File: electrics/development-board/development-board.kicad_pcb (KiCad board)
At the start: 2 copper layers, 153 x 77 mm, 103 parts, among them J1 East, J10 Ext_5V, J2 Screw_Terminal, J3 USB_B, J4 Keyboard, J5 Mouse, J6 Audio, J7 VGA, J8 West, J9 PinOut, Q1 MMBT3904, Q2 MMBT3904, Q3 S8050, Q4 S8050, SW1 Reset, SW2 Setup, SW3 Power, U1 LD1117S33, U2 FT2232HL, U3 93C46-WMN6TP, U4 LTV-817S, U5 LTV-817S, U6 MAX3486, U7 SN74CBT16292, U8 SN74CBT16292, Y1 12MHz

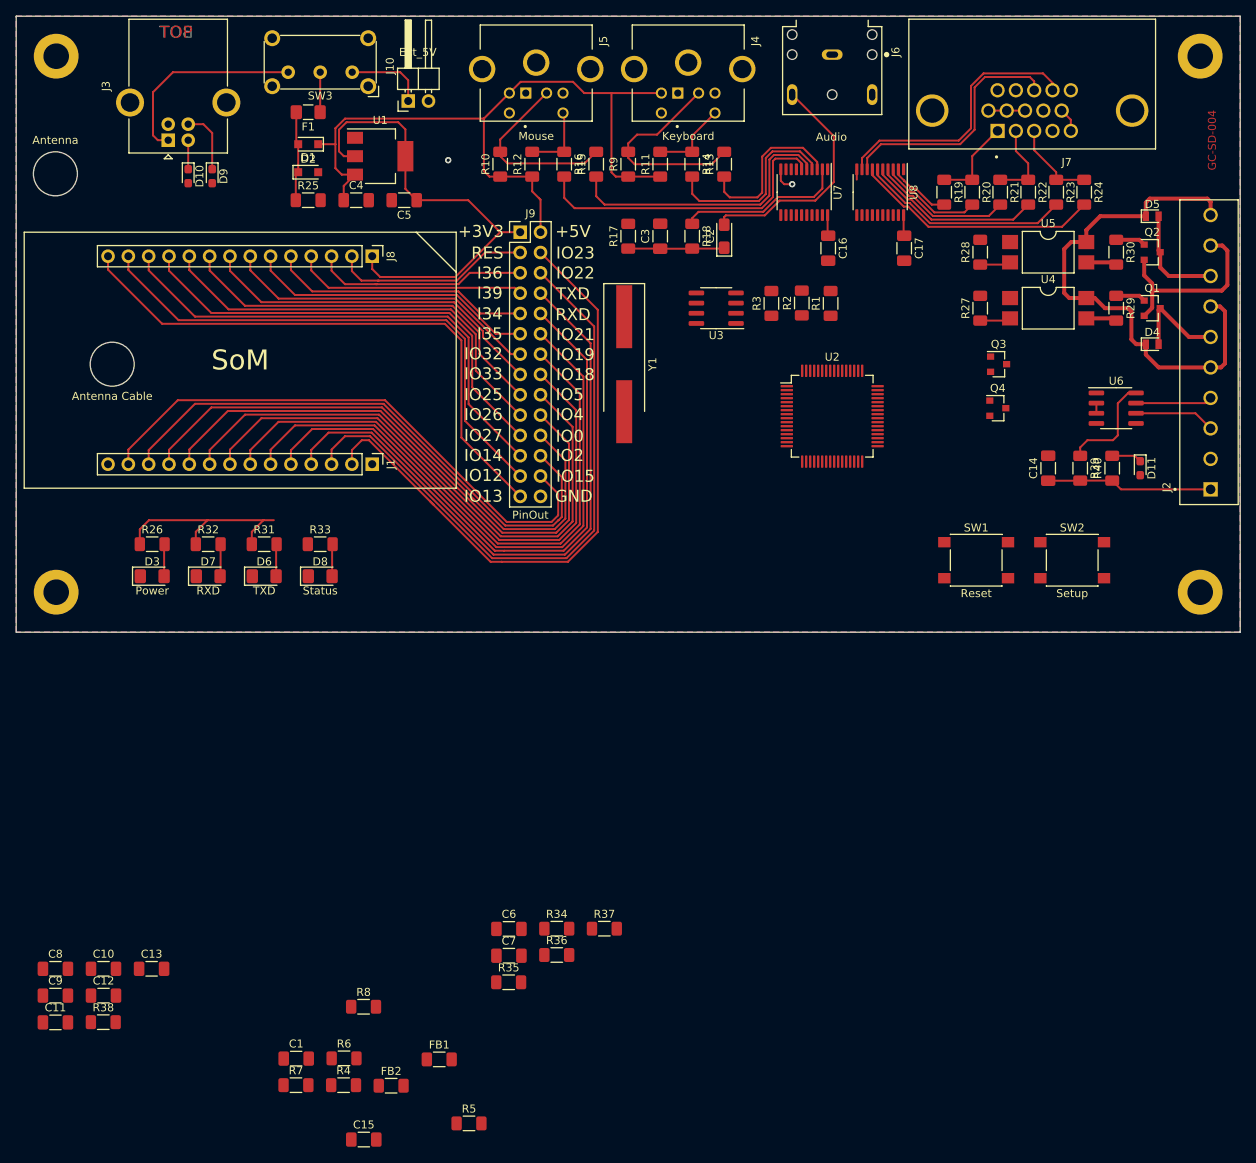
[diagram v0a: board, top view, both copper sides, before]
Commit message: Fix all ERC and DRC warnings during build
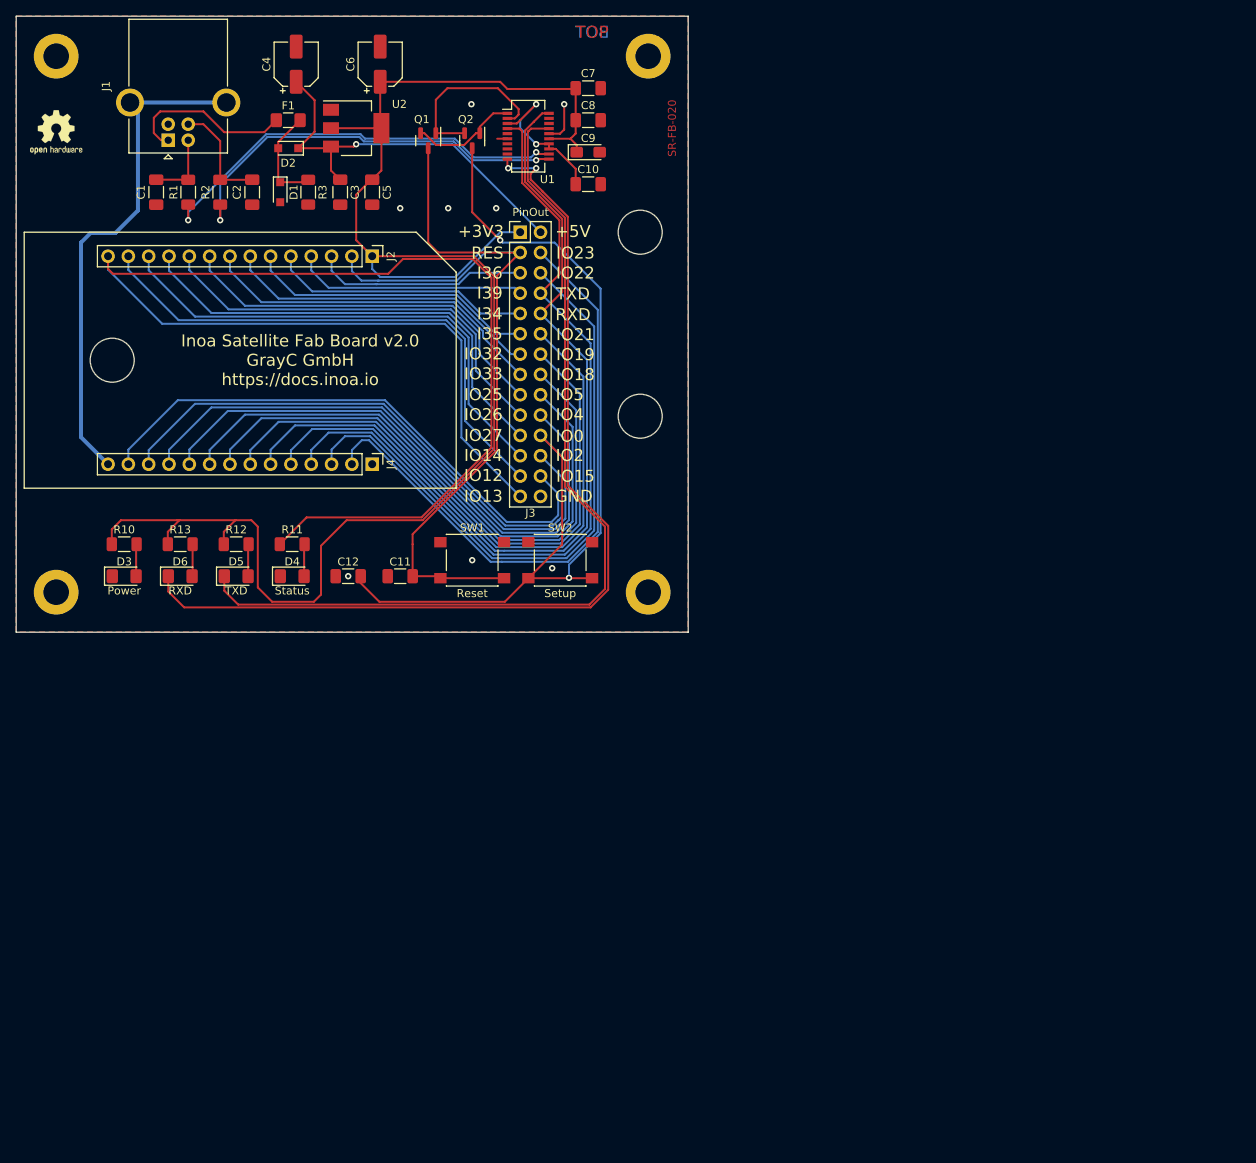
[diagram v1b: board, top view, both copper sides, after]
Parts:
- removed the C11 at (54.9, 175.8)
- removed the C12 at (60.9, 172.4)
- removed C13: 0u1, Capacitor_SMD:C_1206_3216Metric_Pad1.33x1.80mm_HandSolder
- removed C14, C15, C16, C17: 100nF, Capacitor_SMD:C_1206_3216Metric_Pad1.33x1.80mm_HandSolder
- removed the C3 at (130.5, 77.5)
- removed D10, D11, D9: D_TVS, Diode_SMD:D_0603_1608Metric_Pad1.05x0.95mm_HandSolder
- removed the D4 at (192.0, 91.0)
- removed the D5 at (192.0, 75.0)
- removed FB1, FB2: 1k@100MHz, Resistor_SMD:R_1206_3216Metric_Pad1.30x1.75mm_HandSolder
- removed J10: Ext_5V, Connector_PinHeader_2.54mm:PinHeader_1x02_P2.54mm_Horizontal
- removed the J2 at (199.3, 92.0)
- removed the J3 at (69.0, 65.5)
- removed the J4 at (134.0, 55.8)
- removed J5: Mouse, footprints:TE_5749180-1
- removed J6: Audio, footprints:CUI_SJ1-3523N
- removed J7: VGA, footprints:AMPHENOL_L77HDE15SD1CH4F
- removed Q3, Q4: S8050, Package_TO_SOT_SMD:SOT-23
- removed the R10 at (110.5, 68.5)
- removed the R11 at (130.5, 68.5)
- removed the R12 at (114.5, 68.5)
- removed the R13 at (138.5, 68.5)
- removed R14, R15, R16: 120R, Resistor_SMD:R_1206_3216Metric_Pad1.30x1.75mm_HandSolder
- removed R17: 150R, Resistor_SMD:R_1206_3216Metric_Pad1.30x1.75mm_HandSolder
- removed R18: 270R, Resistor_SMD:R_1206_3216Metric_Pad1.30x1.75mm_HandSolder
- removed R19, R21, R23: 400R, Resistor_SMD:R_1206_3216Metric_Pad1.30x1.75mm_HandSolder
- removed R20, R22, R24: 800R, Resistor_SMD:R_1206_3216Metric_Pad1.30x1.75mm_HandSolder
- removed R27, R28, R29, R30: 220R, Resistor_SMD:R_1206_3216Metric_Pad1.30x1.75mm_HandSolder
- removed the R3 at (144.4, 85.9)
- removed R34, R35, R36, R37, R4, R5, R7: 10k, Resistor_SMD:R_1206_3216Metric_Pad1.30x1.75mm_HandSolder
- removed R38: 12k, Resistor_SMD:R_1206_3216Metric_Pad1.30x1.75mm_HandSolder
- removed R39, R40: R, Resistor_SMD:R_1206_3216Metric_Pad1.30x1.75mm_HandSolder
- removed R6: 2k2, Resistor_SMD:R_1206_3216Metric_Pad1.30x1.75mm_HandSolder
- removed R8: 0R, Resistor_SMD:R_1206_3216Metric_Pad1.30x1.75mm_HandSolder
- removed R9: 2k, Resistor_SMD:R_1206_3216Metric_Pad1.30x1.75mm_HandSolder
- removed SW3: Power, Button_Switch_THT:SW_E-Switch_EG1224_SPDT_Angled
- removed U3: 93C46-WMN6TP, Package_SO:SOIC-8_3.9x4.9mm_P1.27mm
- removed U4, U5: LTV-817S, Package_DIP:SMDIP-4_W9.53mm
- removed U6: MAX3486, Package_SO:SOIC-8_3.9x4.9mm_P1.27mm
- removed U7, U8: SN74CBT16292, Package_SO:TSSOP-20_4.4x6.5mm_P0.65mm
- removed Y1: 12MHz, Crystal:Crystal_SMD_HC49-SD_HandSoldering
- added C4: 100uF, Capacitor_SMD:CP_Elec_5x5.3, F.Cu at (85.0, 56.0)
- added C6: 47uF, Capacitor_SMD:CP_Elec_5x5.3, F.Cu at (95.5, 56.0)
- added C9: 4u7, Capacitor_Tantalum_SMD:CP_EIA-3216-18_Kemet-A_Pad1.58x1.35mm_HandSolder, F.Cu at (121.5, 67.0)
- added H5: Antenna, MountingHole:MountingHole_5.5mm, F.Cu at (128.0, 100.0)
- added J1: USB_B, Connector_USB:USB_B_OST_USB-B1HSxx_Horizontal, F.Cu at (69.0, 65.5)
- added LOGO1: Logo_Open_Hardware_Small, Symbol:OSHW-Logo2_7.3x6mm_SilkScreen, F.Cu at (55.0, 64.5)
- added LOGO2: LOGO, images:grayc-logo-negative, F.Cu at (55.0, 71.0)
- C1: value 100nF -> 47pF
- C10: value 4u7 -> 100nF
- C11: renamed from C6; value C -> 1nF
- C12: renamed from C7; value C -> 1nF
- C2: value 10uF -> 47pF; footprint Capacitor_Tantalum_SMD:CP_EIA-3216-18_Kemet-A_Pad1.58x1.35mm_HandSolder -> Capacitor_SMD:C_1206_3216Metric_Pad1.33x1.80mm_HandSolder
- C7: renamed from C8; value 12pF -> 100nF
- C8: renamed from C9; value 12pF -> 100nF
- F1: value 6V/800mA -> 1A
- H7: renamed from H5; value Antenna Cable -> WiFi Cable
- Q1, Q2: value MMBT3904 -> S8050
- R1, R2: value 33R -> 27R
- U1: renamed from U2; value FT2232HL -> FT231XS; footprint Package_QFP:LQFP-64_10x10mm_P0.5mm -> Package_SO:SSOP-20_3.9x8.7mm_P0.635mm
- moved C7 128.7 mm to (121.5, 59.0)
- moved C8 128.1 mm to (121.5, 63.0)
- moved C10 115.3 mm to (121.5, 71.0)
- moved C1 109.7 mm to (67.5, 72.0), turned to -90 degrees
- moved Q1 92.9 mm to (101.5, 65.6), turned to -90 degrees
- moved Q2 86.1 mm to (107.0, 65.6), turned to -90 degrees
- moved R1 81.5 mm to (71.5, 72.0)
- moved R2 74.0 mm to (75.5, 72.0)
- moved H6 73.5 mm to (128.0, 77.0)
- moved H3 69.0 mm to (129.0, 122.0)
- moved H4 69.0 mm to (129.0, 55.0)
- moved SW2 64.0 mm to (118.0, 118.0)
- moved SW1 63.0 mm to (107.0, 118.0)
- moved C2 59.3 mm to (79.5, 72.0), turned to -90 degrees
- moved U1 51.7 mm to (114.0, 65.0)
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- renumbered C4 to C3, D8 to D4, D6 to D5, D7 to D6, H4 to H3, H3 to H4, J8 to J2, J9 to J3, J1 to J4, R26 to R10, R33 to R11, R31 to R12, R32 to R13, R25 to R3, U1 to U2
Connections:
- net I34 renamed Net-(J2-Pad5)
- net I35 renamed Net-(J2-Pad6)
- net I36 renamed Net-(J2-Pad3)
- net I39 renamed Net-(J2-Pad4)
- net IO12 renamed Net-(J2-Pad13)
- net IO13 renamed STATUS_LED
- net IO14 renamed Net-(J2-Pad12)
- net IO15 renamed Net-(J3-Pad26)
- net IO18 renamed Net-(J3-Pad16)
- net IO19 renamed Net-(J3-Pad14)
- net IO2 renamed Net-(J3-Pad24)
- net IO21 renamed Net-(J3-Pad12)
- net IO22 renamed Net-(J3-Pad6)
- net IO23 renamed Net-(J3-Pad4)
- net IO25 renamed Net-(J2-Pad9)
- net IO26 renamed Net-(J2-Pad10)
- net IO27 renamed Net-(J2-Pad11)
- net IO32 renamed Net-(J2-Pad7)
- net IO33 renamed Net-(J2-Pad8)
- net IO4 renamed Net-(J3-Pad20)
- net IO5 renamed Net-(J3-Pad18)
- C1 pad 1: +3V3 -> USB_DN
- C10 pad 1: Net-(C10-Pad1) -> VCCIO
- C2 pad 1: Net-(C2-Pad1) -> USB_DP
- C2 pad 2: Net-(C2-Pad2) -> GND
- C3 pad 1: +5V -> VBUS
- C7 pad 1: Net-(C8-Pad1) -> +3V3
- C8 pad 1: Net-(C9-Pad1) -> +3V3
- D2 pad 1: +5V -> VBUS
- D5 pad 1: TX_LED -> TXD_LED
- D6 pad 1: RX_LED -> RXD_LED
- J3 pad 2: +5V -> VBUS
- Q1 pad 1: Net-(Q1-Pad1) -> FT_~{RTS}
- Q1 pad 2: GND2 -> FT_~{DTR}
- Q1 pad 3: Relay_In_0 -> Chip_PU
- Q2 pad 1: Net-(Q2-Pad1) -> FT_~{DTR}
- Q2 pad 2: GND2 -> FT_~{RTS}
- Q2 pad 3: Relay_In_1 -> IO0
- R1 pad 1: EECS -> Net-(R1-Pad1)
- R1 pad 2: Net-(R1-Pad2) -> USB_DN
- R2 pad 1: EECLK -> Net-(R2-Pad1)
- R2 pad 2: Net-(R2-Pad2) -> USB_DP
- U1 pad 1: GND -> FT_~{DTR}
- U1 pad 10: GND -> RXD_LED
- U1 pad 11: GND -> Net-(R2-Pad1)
- U1 pad 12: Net-(U2-Pad12) -> Net-(R1-Pad1)
- U1 pad 13: GND -> VCCIO
- U1 pad 14: Net-(U2-Pad14) -> VCCIO
- U1 pad 15: GND -> +3V3
- U1 pad 16: FT_TCK -> GND
- U1 pad 17: FT_TDI -> TXD_LED
- U1 pad 18: FT_TDO -> unconnected-(U1-Pad18)
- U1 pad 19: FT_TMS -> unconnected-(U1-Pad19)
- U1 pad 2: Net-(C8-Pad1) -> FT_~{RTS}
- U1 pad 20: Net-(U2-Pad20) -> U0RXD
- U1 pad 3: Net-(C9-Pad1) -> VCCIO
- U1 pad 4: Net-(C10-Pad1) -> U0TXD
- U1 pad 5: GND -> unconnected-(U1-Pad5)
- U1 pad 6: Net-(R38-Pad1) -> GND
- U1 pad 7: USB_DN -> unconnected-(U1-Pad7)
- U1 pad 8: USB_DP -> unconnected-(U1-Pad8)
- U1 pad 9: Net-(C12-Pad1) -> unconnected-(U1-Pad9)
- U2 pad 3: +5V -> VBUS
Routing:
- net RXD_LED: track 0.00 -> 120.3 mm, vias 0 -> 2
- net IO0: track 72.1 -> 190.6 mm, vias 0 -> 2
- net TXD_LED: track 0.00 -> 114.9 mm
- net STATUS_LED: track 72.1 -> 176.2 mm
- net +3V3: track 103.1 -> 205.0 mm
- net +5V: track 94.0 -> 0.00 mm
- net Chip_PU: track 24.9 -> 106.3 mm
- net VS: track 65.6 -> 0.00 mm
- net GND: track 11.9 -> 70.4 mm, vias 2 -> 8
- net Net-(R1-Pad1): track 0.00 -> 53.6 mm, vias 0 -> 2
- net Net-(R2-Pad1): track 0.00 -> 51.3 mm, vias 0 -> 2
- net PS2_1_Data: track 39.1 -> 0.00 mm
- net PS2_1_Clock: track 35.6 -> 0.00 mm
- net VSync: track 34.1 -> 0.00 mm
- net Blue_Low: track 31.0 -> 0.00 mm
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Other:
- board size 153 x 77 mm -> 84 x 77 mm
- board text added: "Inoa Satellite Fab Board v2.0 GrayC GmbH https://docs.inoa.io"
- board text added: "SR-FB-020"
- board text removed: "GC-SD-004"
- board text removed: "SoM"
